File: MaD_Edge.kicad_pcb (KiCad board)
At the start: 4 copper layers, 144.1 x 93.3 mm, 280 parts, among them IC1 ISO6742DWR, IC10 NSI50010YT1G, IC11 NSI50010YT1G, IC12 NSI50010YT1G, IC13 NSI50010YT1G, IC14 ISO6741DWR, IC15 ISO6721BDR, IC16 ISO6740FDWR, IC2 ISO6742DWR, IC3 UCC12040DVER, IC4 UCC12040DVER, IC5 ISO6731DWR, IC6 NSI50010YT1G, IC7 NSI50010YT1G, IC8 NSI50010YT1G, IC9 NSI50010YT1G, J1 Debug, J10 ChargePump, J11 ESDUpper, J12 ESDLower, J13 ESDActive, J14 ENDUpper, J15 ENDLower, J16 Door, J17 GPI_3, J18 GPI_4, J19 NavKey, J2 Main_Power, J20 Encoder, J21 ServoCtrl, J22 GPIO_EXT_1, J23 ServoSerial, J24 GPIO_EXT_2, J3 P2_EDGE_MODULE_SOCKET, J4 RPI, J5 GPO_2, J6 GPO_1, J7 GPI_2, J8 GPI_1, J9 Force, Q1 NPN, SW1 RESET, U1 XL1509-5V, U10 SN74LVC1G14DBV, U11 SN74LVC1G14DBV, U12 SN74LVC1G14DBV, U13 SN74LVC1G14DBV, U14 SN74LVC1G14DBV, U15 SN74LVC1G14DBV, U16 SN74LVC1G14DBV, U17 SN74LVC1G14DBV, U18 SN74LVC1G14DBV, U19 SN74LVC1G14DBV, U2 XL1509-3.3V, U21 SN74LVC1G14DBV, U22 SN74LVC1G14DBV, U24 AM26LS31CD, U25 AM26LV32xD, U27 SN74LVC1G14DBV, U28 SN74LVC1G14DBV, U29 SN74LVC1G14DBV, U3 APM4953, U30 SN74LVC1G14DBV, U31 SN74LVC1G14DBV, U32 SN74LVC1G14DBV, U33 SN74LVC1G14DBV, U34 SN74LVC1G14DBV, U4 6N137, U5 VO2631, U6 VO2631, U7 VO2631, U8 VO2631, U9 SN74LVC1G14DBV

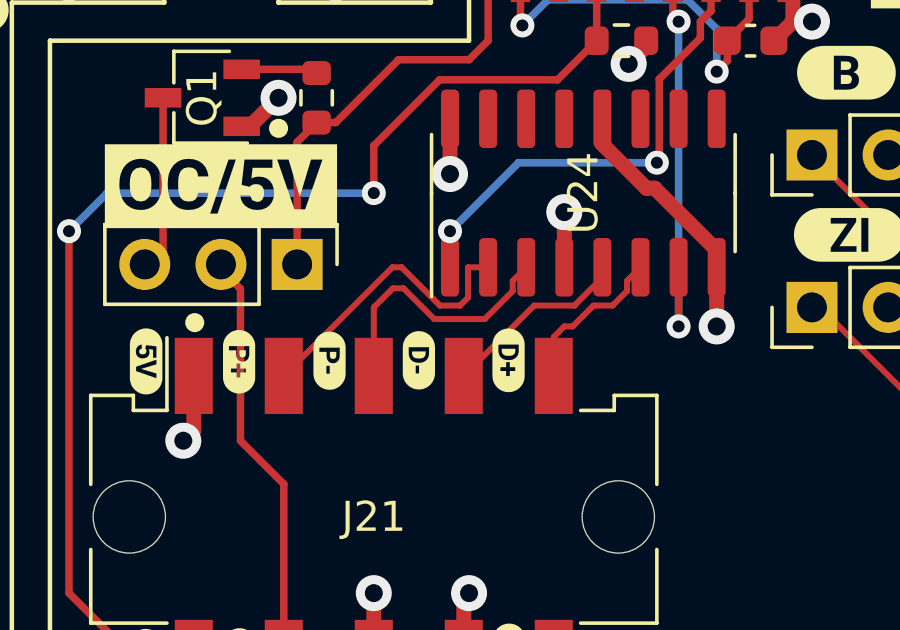
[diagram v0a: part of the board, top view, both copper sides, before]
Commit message: working version for getting basic data for the thesis
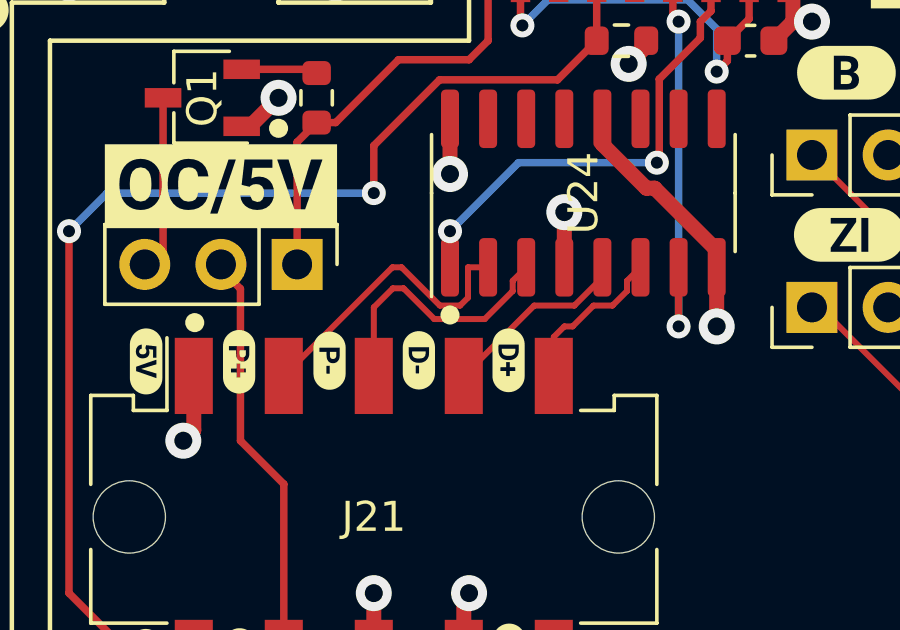
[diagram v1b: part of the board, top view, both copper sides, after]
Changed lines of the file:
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@@
   (gr_line (start 109.22 118.11) (end 109.22 132.08)
     (stroke (width 0.15) (type solid)) (layer "F.SilkS"))
+  (gr_circle (center 27.305 195.834) (end 27.522849 195.834)
+    (stroke (width 0.2) (type solid)) (fill solid) (layer "F.SilkS"))
   (gr_circle (center 108.331 159.004) (end 108.548849 159.004)
     (stroke (width 0.2) (type solid)) (fill solid) (layer "F.SilkS"))
